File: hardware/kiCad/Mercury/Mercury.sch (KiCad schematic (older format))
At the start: 55 parts

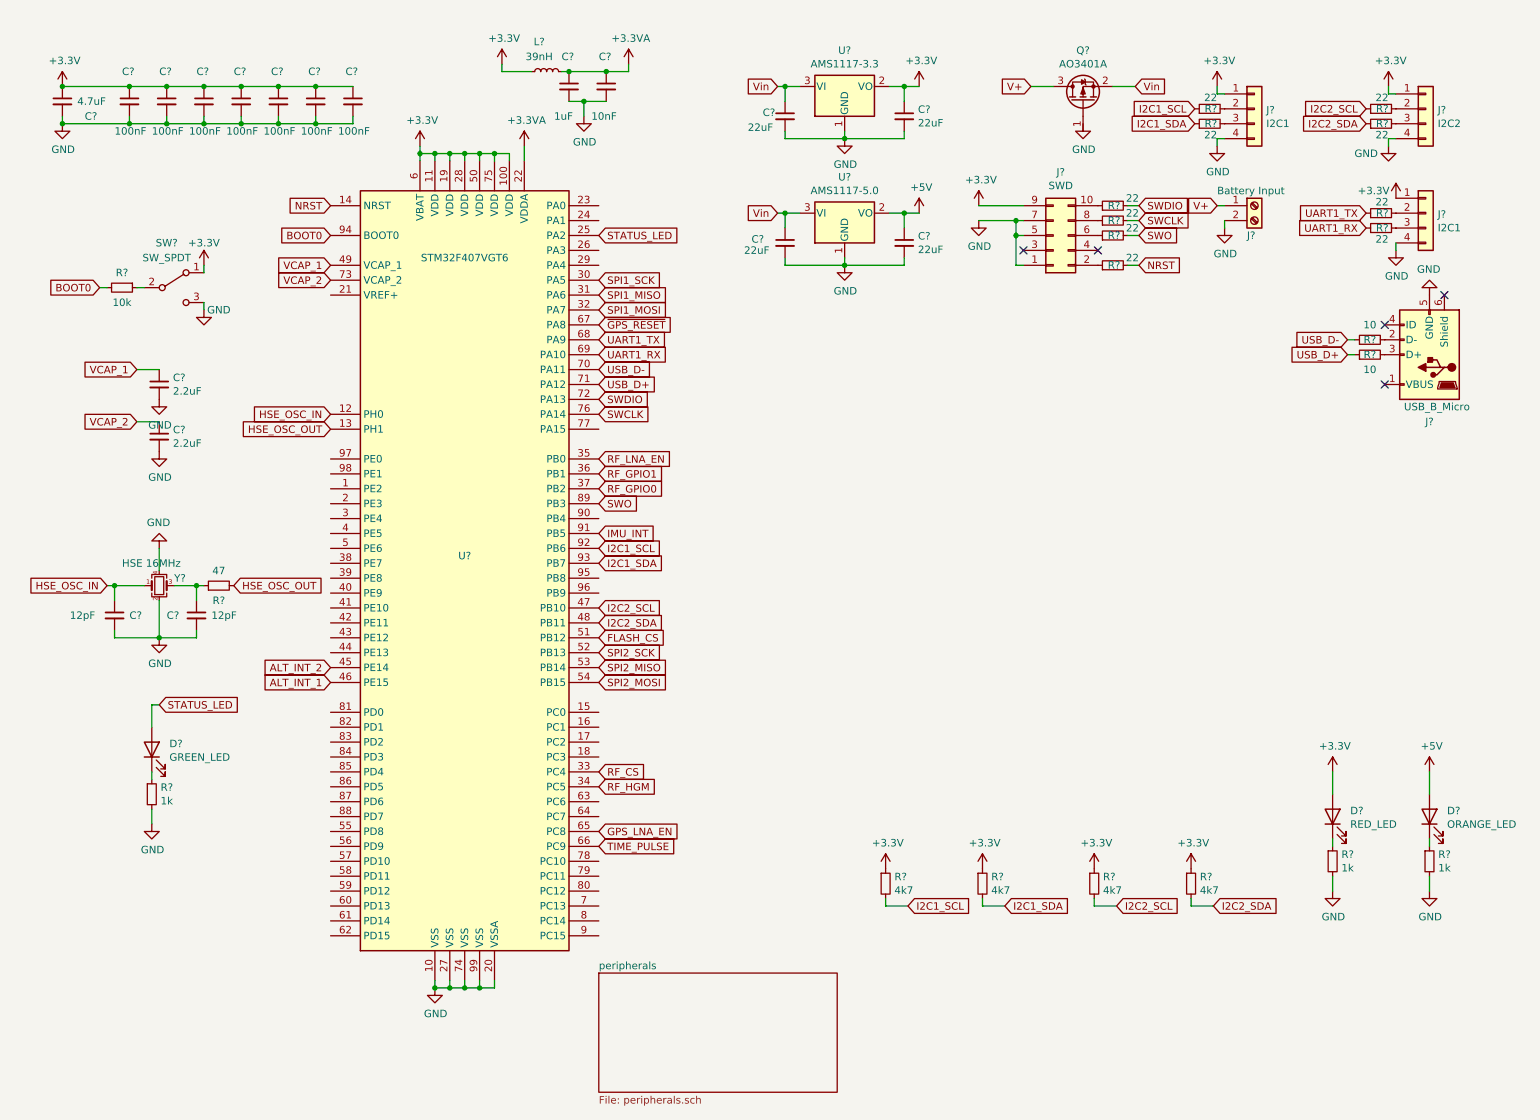
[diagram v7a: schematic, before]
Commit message: Footprints Assigned, Schematic Finalized
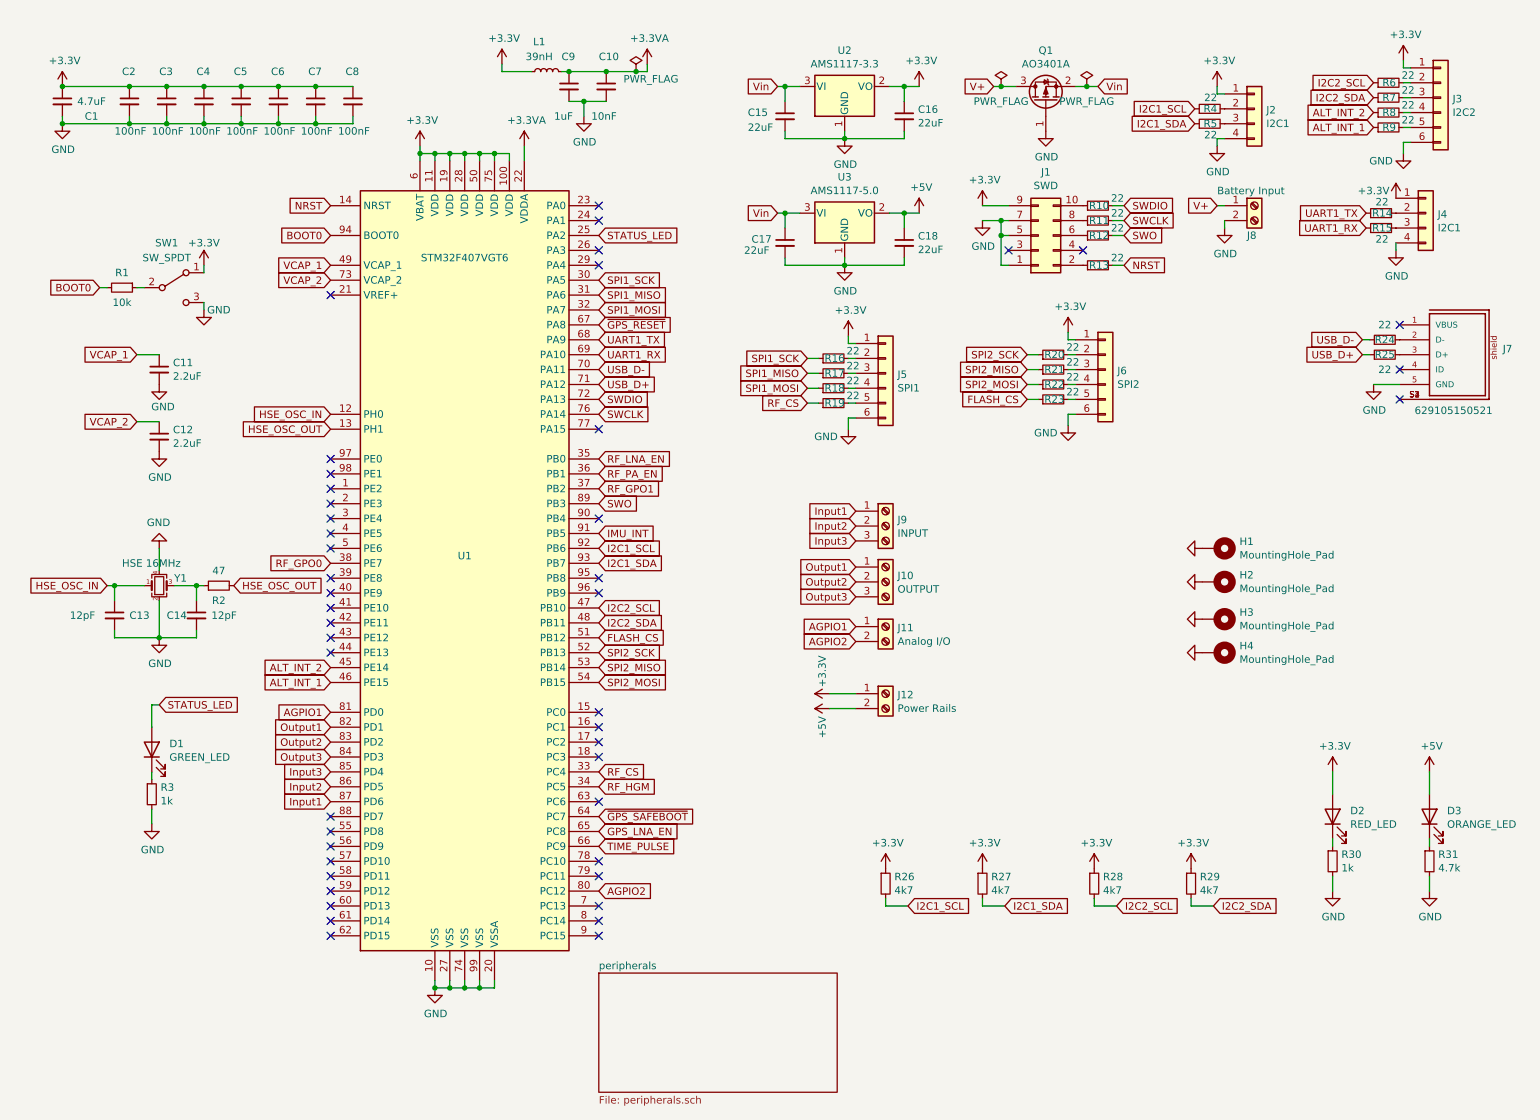
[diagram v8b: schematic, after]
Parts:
- removed J?: USB_B_Micro, symbol Connector:USB_B_Micro
- removed J?: I2C2, symbol Connector_Generic:Conn_01x04
- added H1, H2, H3, H4: MountingHole_Pad, MountingHole:MountingHole_4.3mm_M4_Pad_Via, symbol Mechanical:MountingHole_Pad
- added J10: OUTPUT, TerminalBlock_Phoenix:TerminalBlock_Phoenix_MKDS-1,5-3-5.08_1x03_P5.08mm_Horizontal, symbol Connector:Screw_Terminal_01x03
- added J11: Analog I/O, TerminalBlock_Phoenix:TerminalBlock_Phoenix_MKDS-1,5-2-5.08_1x02_P5.08mm_Horizontal, symbol Connector:Screw_Terminal_01x02
- added J12: Power Rails, TerminalBlock_Phoenix:TerminalBlock_Phoenix_MKDS-1,5-2-5.08_1x02_P5.08mm_Horizontal, symbol Connector:Screw_Terminal_01x02
- added J3: I2C2, Connector_Wire:SolderWire-0.25sqmm_1x04_P4.2mm_D0.65mm_OD1.7mm, symbol Connector_Generic:Conn_01x06
- added J5: SPI1, Connector_Wire:SolderWire-0.25sqmm_1x05_P4.5mm_D0.65mm_OD2mm, symbol Connector_Generic:Conn_01x06
- added J6: SPI2, Connector_Wire:SolderWire-0.25sqmm_1x05_P4.5mm_D0.65mm_OD2mm, symbol Connector_Generic:Conn_01x06
- added J7: 629105150521, 629105150521:629105150521, symbol 629105150521:629105150521
- added J9: INPUT, TerminalBlock_Phoenix:TerminalBlock_Phoenix_MKDS-1,5-3-5.08_1x03_P5.08mm_Horizontal, symbol Connector:Screw_Terminal_01x03
- added R16, R17, R18, R19, R20, R21, R22, R23, R8, R9: 22, Resistor_SMD:R_0402_1005Metric, symbol Device:R_Small
- C1, C15, C16, C17, C18: renamed from C?; footprint (none) -> Capacitor_SMD:C_0805_2012Metric
- C10, C13, C14, C9: renamed from C?; footprint (none) -> Capacitor_SMD:C_0402_1005Metric
- C11, C12, C2, C3, C4, C5, C6, C7, C8: renamed from C?; footprint (none) -> Capacitor_SMD:C_0603_1608Metric
- D1, D2, D3: renamed from D?; footprint (none) -> LED_SMD:LED_0603_1608Metric
- J1: renamed from J?; footprint (none) -> Connector_PinHeader_1.27mm:PinHeader_2x05_P1.27mm_Vertical
- J2, J4: renamed from J?; footprint (none) -> Connector_Wire:SolderWire-0.25sqmm_1x04_P4.2mm_D0.65mm_OD1.7mm
- J8: renamed from J?; footprint (none) -> TerminalBlock_Phoenix:TerminalBlock_Phoenix_MKDS-3-2-5.08_1x02_P5.08mm_Horizontal
- L1: renamed from L?; footprint (none) -> Inductor_SMD:L_0402_1005Metric
- R1, R10, R11, R12, R13, R14, R15, R26, R27, R28, R29, R3, R30, R4, R5, R6, R7: renamed from R?; footprint (none) -> Resistor_SMD:R_0402_1005Metric
- R2: renamed from R?; footprint (none) -> Resistor_SMD:R_0805_2012Metric
- R24, R25: renamed from R?; value 10 -> 22; footprint (none) -> Resistor_SMD:R_0402_1005Metric
- R31: renamed from R?; value 1k -> 4.7k; footprint (none) -> Resistor_SMD:R_0402_1005Metric
- SW1: renamed from SW?; footprint (none) -> Button_Switch_THT:SW_CuK_OS102011MA1QN1_SPDT_Angled
- Y1: renamed from Y?; footprint (none) -> Crystal:Crystal_SMD_3225-4Pin_3.2x2.5mm
- gave numbers to parts that had none: 4
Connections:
- net +3V3: now also J12.1 (Pin_1), J3.1 (Pin_1), J5.1 (Pin_1), J6.1 (Pin_1)
- net +5V: now also J12.2 (Pin_2)
- net ALT_INT_1: now also R9.1
- net ALT_INT_2: now also R8.1
- net FLASH_CS: now also R23.1
- net GND: now also Q1.1 (G), H1.1, H2.1, H3.1, H4.1, J3.6 (Pin_6), J5.6 (Pin_6), J6.6 (Pin_6), J7.5 (GND)
- net RF_CS: now also R19.1
- net SPI1_MISO: now also R17.1
- net SPI1_MOSI: now also R18.1
- net SPI1_SCK: now also R16.1
- net SPI2_MISO: now also R21.1
- net SPI2_MOSI: now also R22.1
- net SPI2_SCK: now also R20.1
- net RF_GPO0: now reaches U1.38 (PE7)
- net ~GPS_SAFEBOOT: now reaches U1.64 (PC7)
- net AGPIO2: now reaches U1.80 (PC12)
- net AGPIO2: now also J11.2 (Pin_2)
- net AGPIO1: now reaches U1.81 (PD0)
- net AGPIO1: now also J11.1 (Pin_1)
- net Output1: now reaches U1.82 (PD1)
- net Output1: now also J10.1 (Pin_1)
- net Output2: now reaches U1.83 (PD2)
- net Output2: now also J10.2 (Pin_2)
- net Output3: now reaches U1.84 (PD3)
- net Output3: now also J10.3 (Pin_3)
- net Input3: now reaches U1.85 (PD4)
- net Input3: now also J9.3 (Pin_3)
- net Input2: now reaches U1.86 (PD5)
- net Input2: now also J9.2 (Pin_2)
- net Input1: now reaches U1.87 (PD6)
- net Input1: now also J9.1 (Pin_1)
- net at R24.2: now also J7.2 (D-)
- net at R25.2: now also J7.3 (D+)
- net at R6.2: now also J3.2 (Pin_2)
- net at R7.2: now also J3.3 (Pin_3)
- net RF_GPIO0 renamed RF_GPO1
- net RF_GPIO1 renamed RF_PA_EN
- new net: J3.4 (Pin_4), R8.2
- new net: J3.5 (Pin_5), R9.2
- new net: J5.2 (Pin_2), R16.2
- new net: J5.3 (Pin_3), R17.2
- new net: J5.4 (Pin_4), R18.2
- new net: J5.5 (Pin_5), R19.2
- new net: J7.S1, J7.S2, J7.S3, J7.S4
- new net: J6.2 (Pin_2), R20.2
- new net: J6.3 (Pin_3), R21.2
- new net: J6.4 (Pin_4), R22.2
- new net: J6.5 (Pin_5), R23.2
- no-connect marks 5 -> 46
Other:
- moved on the sheet: C11, J1, Q1, R10, R11, R12, R13, R24, R25, R6, R7
